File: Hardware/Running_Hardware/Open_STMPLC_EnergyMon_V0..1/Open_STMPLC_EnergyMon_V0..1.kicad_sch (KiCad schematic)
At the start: 103 parts, among them J1 Conn_02x08_Odd_Even, J2 Screw_Terminal_01x03, J3 Screw_Terminal_01x02, J4 Screw_Terminal_01x02, J5 Screw_Terminal_01x02, J6 Screw_Terminal_01x02, U1 ATM90E36A, U5 AMS1117-3.3, Y1 16.384MHz

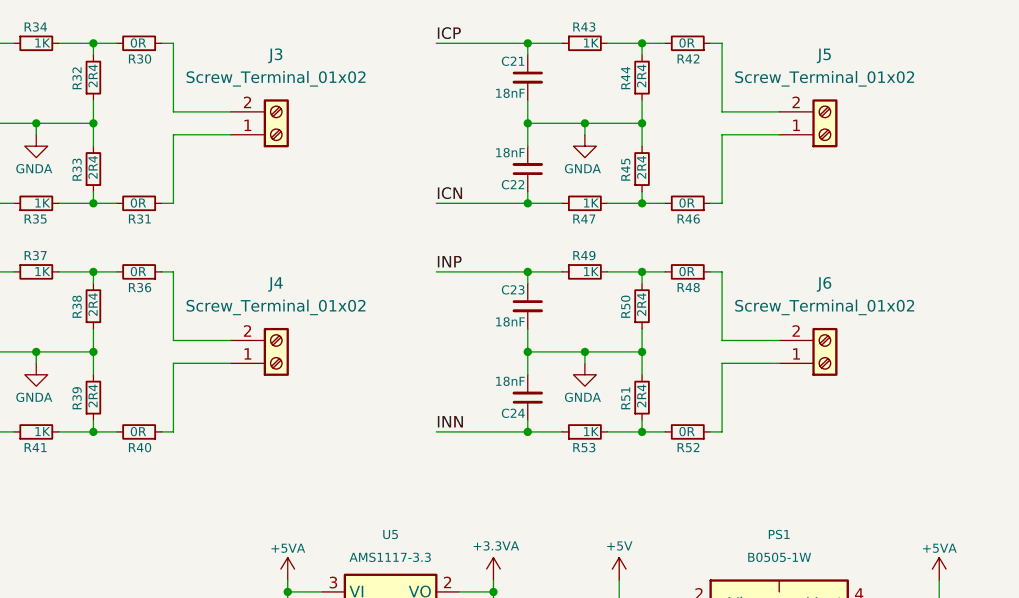
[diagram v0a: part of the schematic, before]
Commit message: CT added
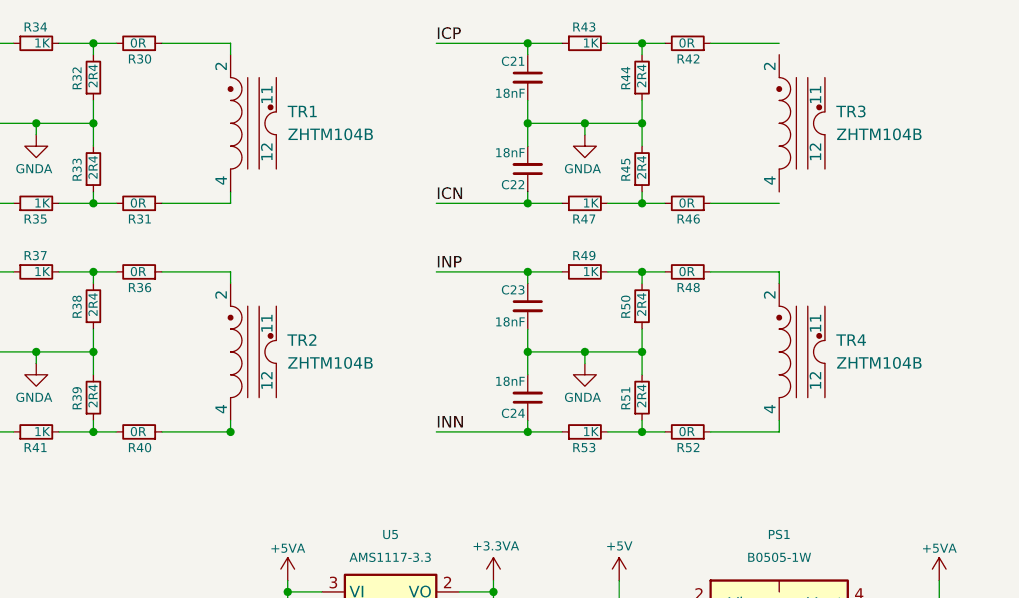
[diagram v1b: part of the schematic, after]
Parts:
- removed J3, J4, J5, J6: Screw_Terminal_01x02, symbol Connector:Screw_Terminal_01x02
- added TR1, TR2, TR3, TR4: ZHTM104B, Transformer_SMD:Transformer_Coilcraft_CST2010, symbol Transformer:CST2010
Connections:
- net at R36.1: now also TR2.2
- net at R31.1: now also TR1.4
- net at R52.1: now also TR4.4
- net at R48.1: now also TR4.2
- net at R30.1: now also TR1.2
- net at R40.1: now also TR2.4

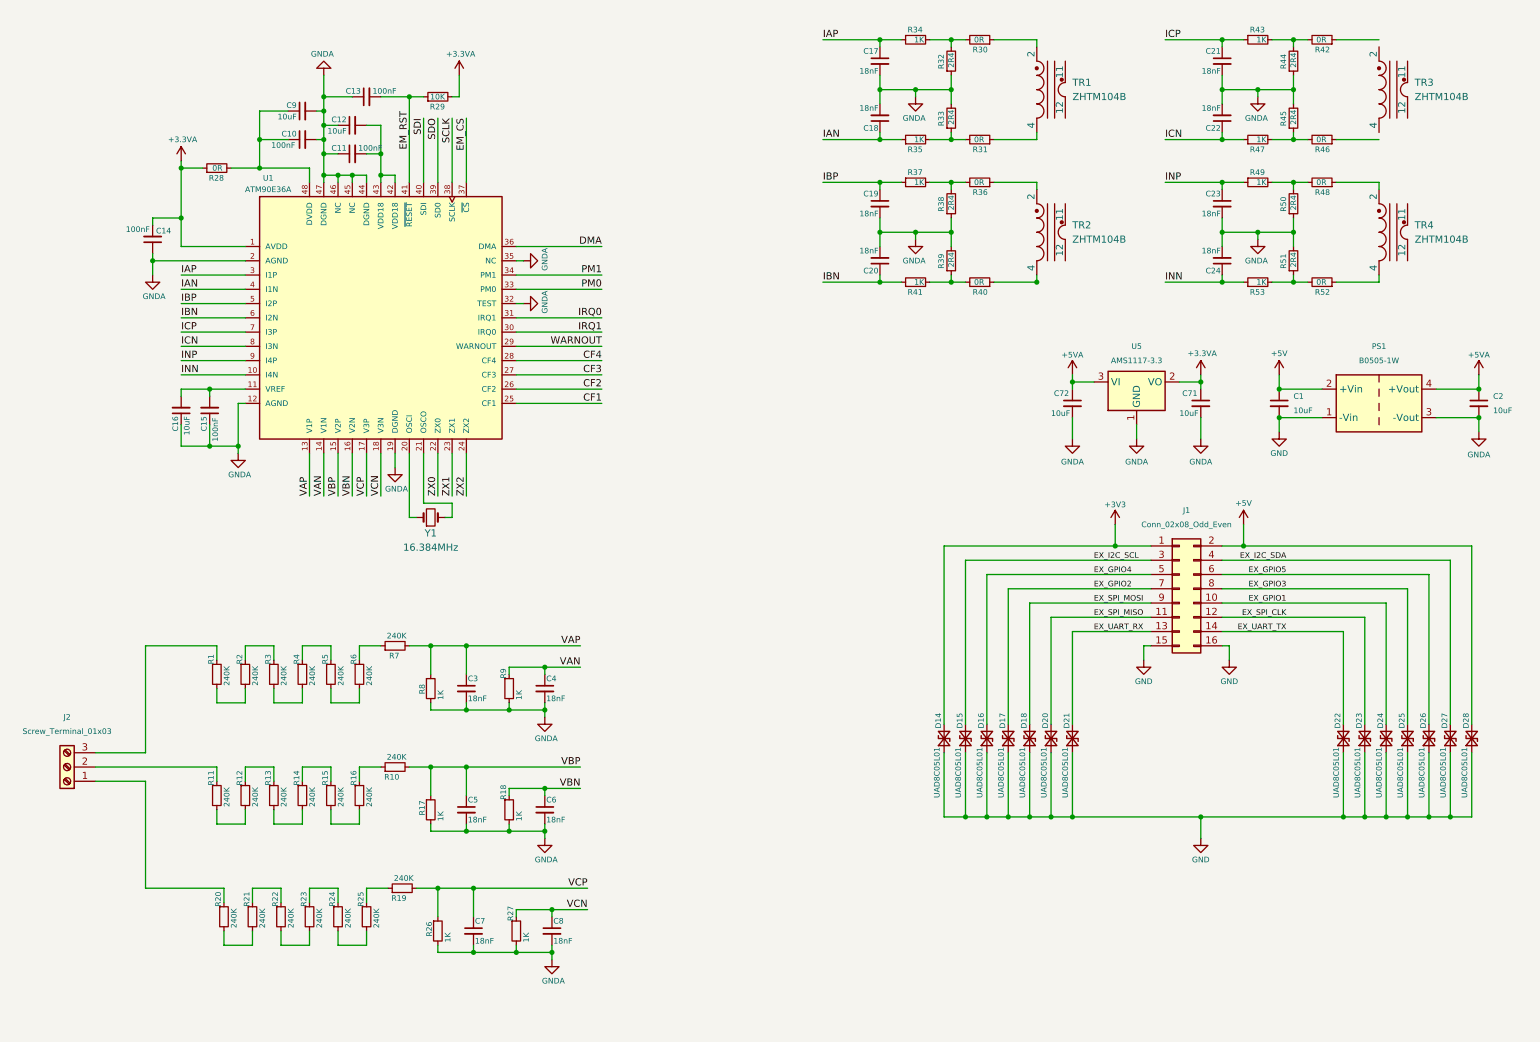
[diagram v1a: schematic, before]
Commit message: Energy monitoring BOM
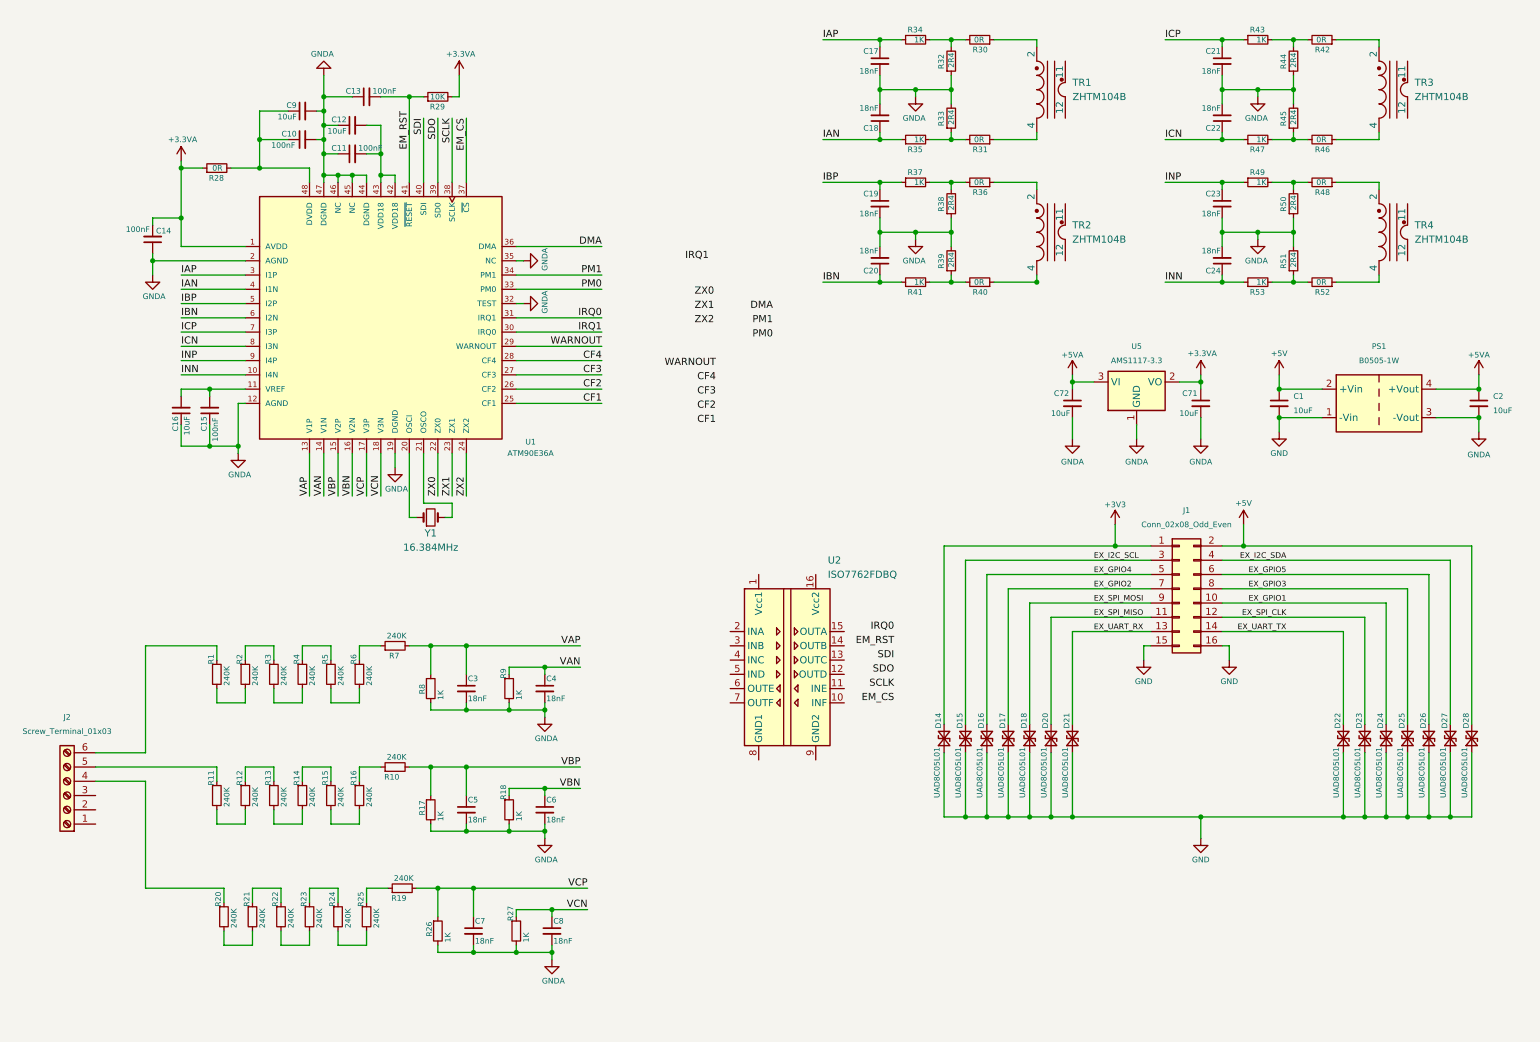
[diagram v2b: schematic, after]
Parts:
- added U2: ISO7762FDBQ, Package_SO:SSOP-16_3.9x4.9mm_P0.635mm, symbol Isolator:ISO7762FDBQ
- C1, C2: footprint (none) -> Capacitor_SMD:C_0805_2012Metric_Pad1.18x1.45mm_HandSolder
- C17, C18, C19, C20, C21, C22, C23, C24, C3, C4, C5, C6, C7, C8: footprint (none) -> Capacitor_SMD:C_0603_1608Metric_Pad1.08x0.95mm_HandSolder
- J2: footprint (none) -> TerminalBlock_Phoenix:TerminalBlock_Phoenix_MKDS-1,5-6-5.08_1x06_P5.08mm_Horizontal; symbol Connector:Screw_Terminal_01x03 -> Connector:Screw_Terminal_01x06
- R1, R10, R11, R12, R13, R14, R15, R16, R17, R18, R19, R2, R20, R21, R22, R23, R24, R25, R26, R27, R28, R29, R3, R30, R31, R34, R35, R36, R37, R4, R40, R41, R42, R43, R46, R47, R48, R49, R5, R52, R53, R6, R7, R8, R9: footprint (none) -> Resistor_SMD:R_0603_1608Metric_Pad0.98x0.95mm_HandSolder
- R32, R33, R38, R39, R44, R45, R50, R51: footprint (none) -> Resistor_SMD:R_0805_2012Metric_Pad1.20x1.40mm_HandSolder
- TR1, TR2, TR3, TR4: footprint Transformer_SMD:Transformer_Coilcraft_CST2010 -> (none)
- Y1: footprint (none) -> Crystal:Crystal_SMD_3225-4Pin_3.2x2.5mm
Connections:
- net at TR3.2: now also R42.1
- net at TR3.4: now also R46.1
- net at J2.1 (Pin_1): no longer R20.1
- net at J2.2 (Pin_2): no longer R11.1
- net at J2.3 (Pin_3): no longer R1.1
- new net: J2.4 (Pin_4), R20.1
- new net: J2.5 (Pin_5), R11.1
- new net: J2.6 (Pin_6), R1.1

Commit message: Energy Monitoring schematic
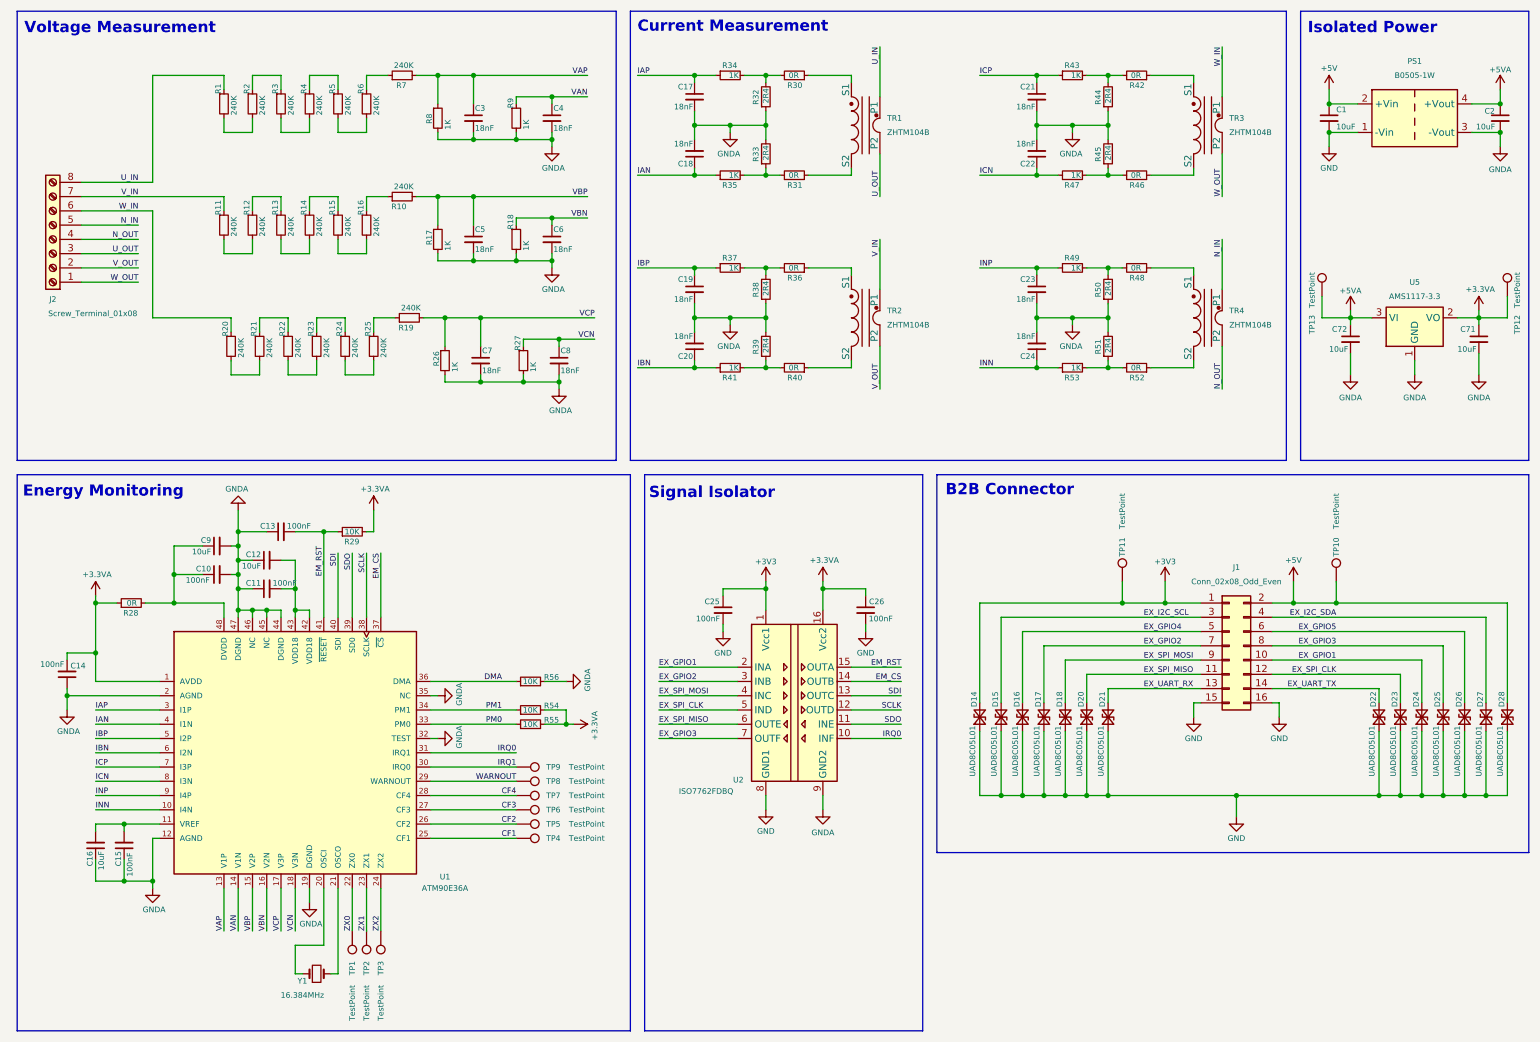
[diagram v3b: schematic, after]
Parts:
- removed J2: Screw_Terminal_01x03, TerminalBlock_Phoenix:TerminalBlock_Phoenix_MKDS-1,5-6-5.08_1x06_P5.08mm_Horizontal, symbol Connector:Screw_Terminal_01x06
- removed TR1, TR2, TR3, TR4: ZHTM104B, symbol Transformer:CST2010
- added C25, C26: 100nF, Capacitor_SMD:C_0603_1608Metric_Pad1.08x0.95mm_HandSolder, symbol Device:C_Small
- added J2: Screw_Terminal_01x08, TerminalBlock_Phoenix:TerminalBlock_Phoenix_MKDS-1,5-8-5.08_1x08_P5.08mm_Horizontal, symbol Connector:Screw_Terminal_01x08
- added R54, R55, R56: 10K, Resistor_SMD:R_0603_1608Metric_Pad0.98x0.95mm_HandSolder, symbol Device:R_Small
- added TP1, TP10, TP11, TP12, TP13, TP2, TP3, TP4, TP5, TP6, TP7, TP8, TP9: TestPoint, TestPoint:TestPoint_Pad_D1.0mm, symbol Connector:TestPoint
- added TR1, TR2, TR3, TR4: ZHTM104B, Footprints:ZHTM104B, symbol ZHTM104B:ZHTM104B
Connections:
- net +3.3VA: now also U2.16 (Vcc2), C26.1, R54.2, R55.2, TP12.1
- net +3V3: now also U2.1 (Vcc1), C25.1, TP11.1
- net +5V: now also TP10.1
- net +5VA: now also TP13.1
- net CF1: now also TP4.1
- net CF2: now also TP5.1
- net CF3: now also TP6.1
- net CF4: now also TP7.1
- net DMA: now also R56.1
- net EM_CS: now also U2.14 (OUTB)
- net EM_RST: now also U2.15 (OUTA)
- net EX_GPIO1: now also U2.2 (INA)
- net EX_GPIO2: now also U2.3 (INB)
- net EX_GPIO3: now also U2.7 (OUTF)
- net EX_SPI_CLK: now also U2.5 (IND)
- net EX_SPI_MISO: now also U2.6 (OUTE)
- net EX_SPI_MOSI: now also U2.4 (INC)
- net GND: now also U2.8 (GND1), C25.2, C26.2
- net GNDA: now also U2.9 (GND2), R56.2
- net IRQ0: now also U2.10 (INF)
- net IRQ1: now also TP9.1
- net PM0: now also R55.1
- net PM1: now also R54.1
- net SCLK: now also U2.12 (OUTD)
- net SDI: now also U2.13 (OUTC)
- net SDO: now also U2.11 (INE)
- net WARNOUT: now also TP8.1
- net ZX0: now also TP1.1
- net ZX1: now also TP2.1
- net ZX2: now also TP3.1
- net at R36.1: now also TR2.S1
- net at R31.1: now also TR1.S2
- net at R42.1: now also TR3.S1
- net at R46.1: now also TR3.S2
- net at R30.1: now also TR1.S1
- net W_IN: now reaches R20.1
- net W_IN: now also J2.6 (Pin_6), TR3.P1
- net V_IN: now reaches R11.1
- net V_IN: now also J2.7 (Pin_7), TR2.P1
- net U_IN: now reaches R1.1
- net U_IN: now also J2.8 (Pin_8), TR1.P1
- net at R48.1: now also TR4.S1
- net at R52.1: now also TR4.S2
- net at R40.1: now also TR2.S2
- new net N_IN: J2.5 (Pin_5), TR4.P1
- new net N_OUT: J2.4 (Pin_4), TR4.P2
- new net U_OUT: J2.3 (Pin_3), TR1.P2
- new net V_OUT: J2.2 (Pin_2), TR2.P2
- new net W_OUT: J2.1 (Pin_1), TR3.P2
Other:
- note added: "B2B Connector"
- note added: "Current Measurement"
- note added: "Energy Monitoring"
- note added: "Isolated Power"
- note added: "Signal Isolator"
- note added: "Voltage Measurement"
- title: (none) -> Open_STMPLC_EnergyMon
- moved on the sheet: C1, C10, C11, C12, C13, C14, C15, C16, C17, C18, C19, C2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
